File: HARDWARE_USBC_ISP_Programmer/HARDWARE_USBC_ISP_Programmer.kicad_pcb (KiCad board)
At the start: 2 copper layers, 9.3 x 7.3 mm, 48 parts, among them J1 105450-0101, J2 Conn_02x03_Odd_Even, J3 Conn_01x10_Female, J4 Conn_01x10_Female, U1 ATmega32U4-M, U2 SMF05CT1G, U3 SMF05CT1G, Y1 16MHz

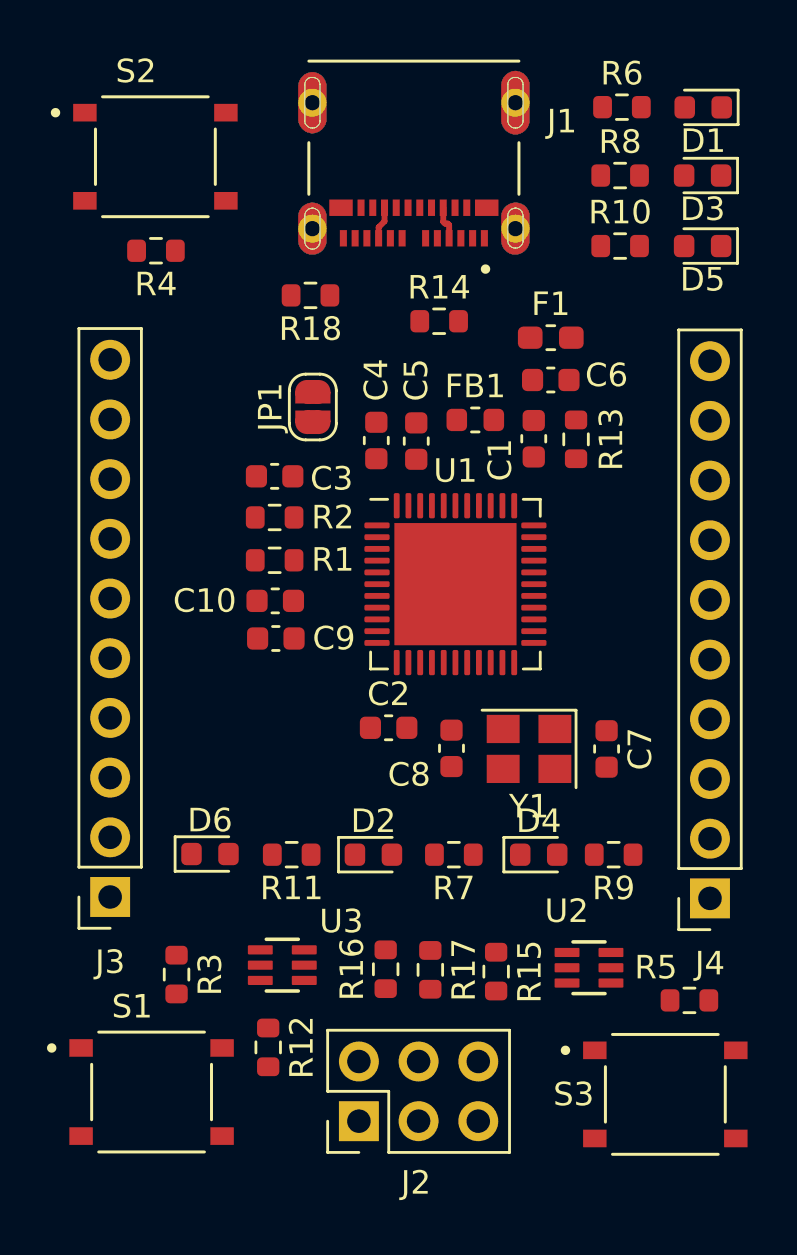
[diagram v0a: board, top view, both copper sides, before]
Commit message: Routed USBC connector
Will need to review, tricky connector to route with small vias, but knowing I am running with USB2 speeds I am not too concerned about impedance and perfect USB3.0 design.

Need to make sure I am within JLC design limits (currently right on the edge)
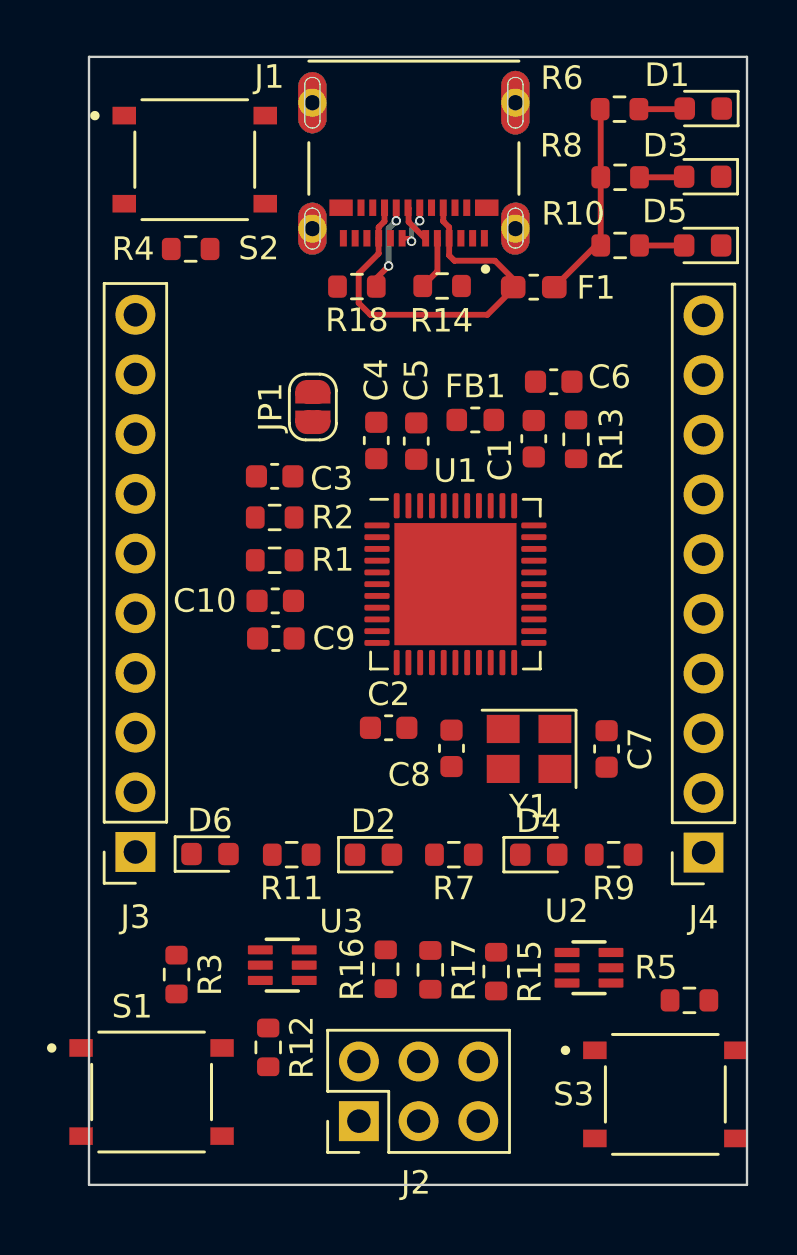
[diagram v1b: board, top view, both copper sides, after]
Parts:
- moved F1 2.27 mm to (77.5, 94.5), turned to 180 degrees
- moved J3 2.20 mm to (60.5, 118.6)
- moved R18 2.01 mm to (70.0, 94.5)
- moved J4 1.97 mm to (84.7, 118.6)
- moved S2 1.68 mm to (63.1, 89.1)
- moved R14 1.51 mm to (73.6, 94.5)
- moved R4 1.48 mm to (62.9, 92.9)
- moved C6 0.15 mm to (78.3, 98.6)
- moved R6 0.13 mm to (81.2, 87.0)
- moved R8 0.08 mm to (81.2, 89.9)
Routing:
- net /USB_VBUS: track 2.88 -> 17.4 mm
- net +5V: track 0.00 -> 8.52 mm
- net /CC2: track 0.00 -> 3.71 mm, vias 0 -> 2
- net /CC1: track 0.00 -> 2.29 mm
- net /USB_D-: track 0.00 -> 2.01 mm, vias 0 -> 2
- net Net-(D1-Pad2): track 0.00 -> 1.96 mm
- net Net-(D3-Pad2): track 0.00 -> 1.91 mm
- net Net-(D5-Pad2): track 0.00 -> 1.90 mm
- net /USB_D+: track 0.00 -> 1.63 mm
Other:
- board size 9.3 x 7.3 mm -> 28 x 48 mm

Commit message: More routing completed
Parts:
- moved D5 5.80 mm to (84.7, 87.0)
- moved R10 5.80 mm to (81.2, 87.0)
- moved FB1 3.40 mm to (76.0, 97.0)
- moved D3 2.90 mm to (84.6, 92.8)
- moved R6 2.90 mm to (81.1, 89.9)
- moved R8 2.90 mm to (81.1, 92.8)
- moved D1 2.90 mm to (84.7, 89.8)
- moved C1 1.79 mm to (78.4, 99.5)
- moved C6 1.79 mm to (79.2, 97.0)
- moved R13 1.72 mm to (80.0, 99.5)
- moved C5 1.29 mm to (72.0, 99.9)
- moved C4 1.25 mm to (70.4, 99.9)
- moved U1 0.86 mm to (74.2, 106.3)
- moved C8 0.33 mm to (73.8, 113.9)
- moved C7 0.29 mm to (80.5, 113.9)
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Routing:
- net /D4: track 0.00 -> 31.0 mm, vias 0 -> 1
- net /TXLED: track 0.00 -> 29.1 mm
- net /D5: track 0.00 -> 28.9 mm, vias 0 -> 1
- net /A5: track 0.00 -> 23.7 mm
- net /A4: track 0.00 -> 23.0 mm
- net +5V: track 8.52 -> 29.8 mm
- net GND: track 0.00 -> 20.0 mm, vias 0 -> 4
- net /IO9: track 0.00 -> 17.1 mm, vias 0 -> 1
- net /D0 / RX: track 0.00 -> 15.7 mm
- net /D1 / TX: track 0.00 -> 13.0 mm
- net /D3 / SCL: track 0.00 -> 12.3 mm, vias 0 -> 1
- net /D2 / SDA: track 0.00 -> 12.1 mm, vias 0 -> 1
- net /HSE_IN: track 0.00 -> 11.0 mm
- net /D6: track 0.00 -> 8.95 mm, vias 0 -> 1
- net /HSE_OUT: track 0.00 -> 8.13 mm
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- added copper zone on In2.Cu, net GND
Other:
- copper layers 2 -> 4

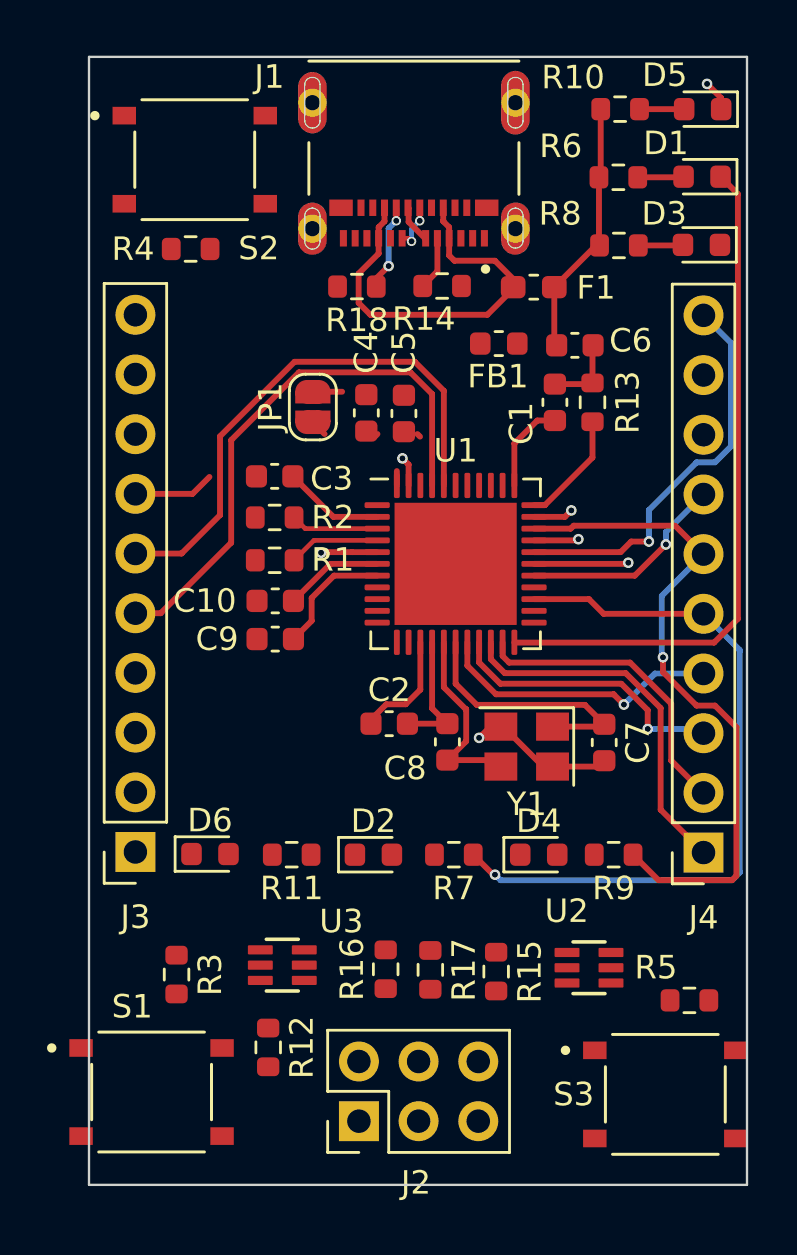
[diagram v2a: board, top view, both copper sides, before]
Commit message: V1 routing complete
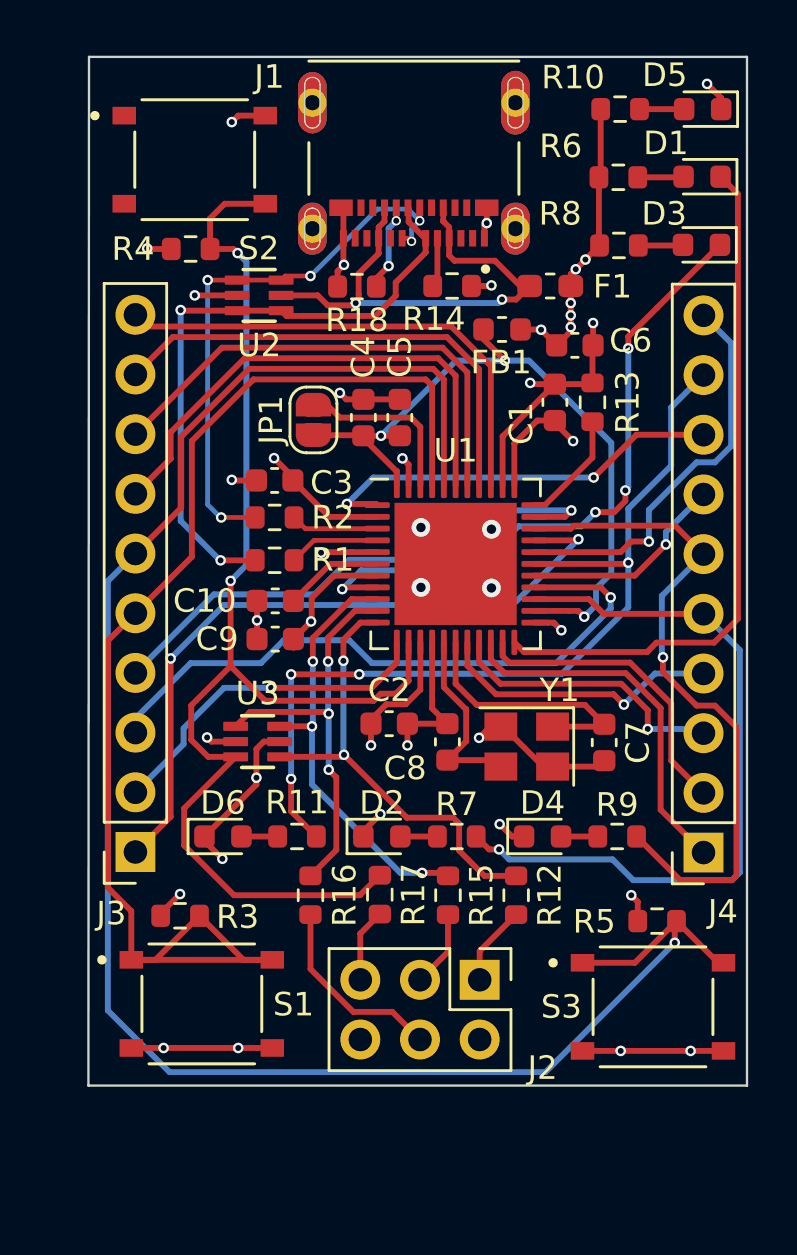
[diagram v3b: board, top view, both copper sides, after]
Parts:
- moved U2 31.9 mm to (65.8, 94.9)
- moved R12 12.4 mm to (76.8, 120.4)
- moved U3 9.57 mm to (65.8, 113.9), turned to 180 degrees
- moved J2 7.91 mm to (75.2, 124.0), turned to -90 degrees
- moved R16 4.49 mm to (68.0, 120.4)
- moved S1 4.32 mm to (63.4, 125.0)
- moved R17 3.86 mm to (71.0, 120.4)
- moved R15 3.84 mm to (73.8, 120.4)
- moved S3 3.76 mm to (82.6, 125.2)
- moved R5 3.64 mm to (82.8, 121.5)
- moved R3 2.50 mm to (62.5, 121.3), turned to 0 degrees
- moved D6 0.93 mm to (64.3, 117.9)
- moved D2 0.85 mm to (71.0, 117.9)
- moved R11 0.81 mm to (67.4, 117.9)
- moved D4 0.79 mm to (77.9, 117.9)
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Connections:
- U3 pad 5: /USB_VBUS -> +5V
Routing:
- net /A4: track 23.0 -> 79.2 mm, vias 0 -> 1
- net /NRESET: track 0.00 -> 53.6 mm, vias 0 -> 2
- net GND: track 20.0 -> 61.0 mm, vias 4 -> 27
- net /IO8: track 4.03 -> 38.2 mm, vias 1 -> 4
- net +5VA: track 1.65 -> 31.2 mm, vias 0 -> 3
- net /A5: track 23.7 -> 53.2 mm
- net /IO10: track 1.91 -> 30.2 mm, vias 1 -> 2
- net /RXLED: track 0.00 -> 27.7 mm, vias 0 -> 4
- net /IO12: track 0.00 -> 27.5 mm, vias 0 -> 1
- net /USB_D+: track 1.63 -> 27.1 mm, vias 0 -> 2
- net /USB_D-: track 2.01 -> 24.4 mm, vias 2 -> 5
- net /IO13: track 1.70 -> 23.1 mm
- net /A0: track 0.00 -> 21.1 mm
- net /A2: track 0.00 -> 20.9 mm
- net /A1: track 0.00 -> 20.8 mm
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- added copper zone on In1.Cu, net +5V
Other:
- board size 28 x 48 mm -> 28 x 43.8 mm
